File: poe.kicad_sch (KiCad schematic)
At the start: 50 parts

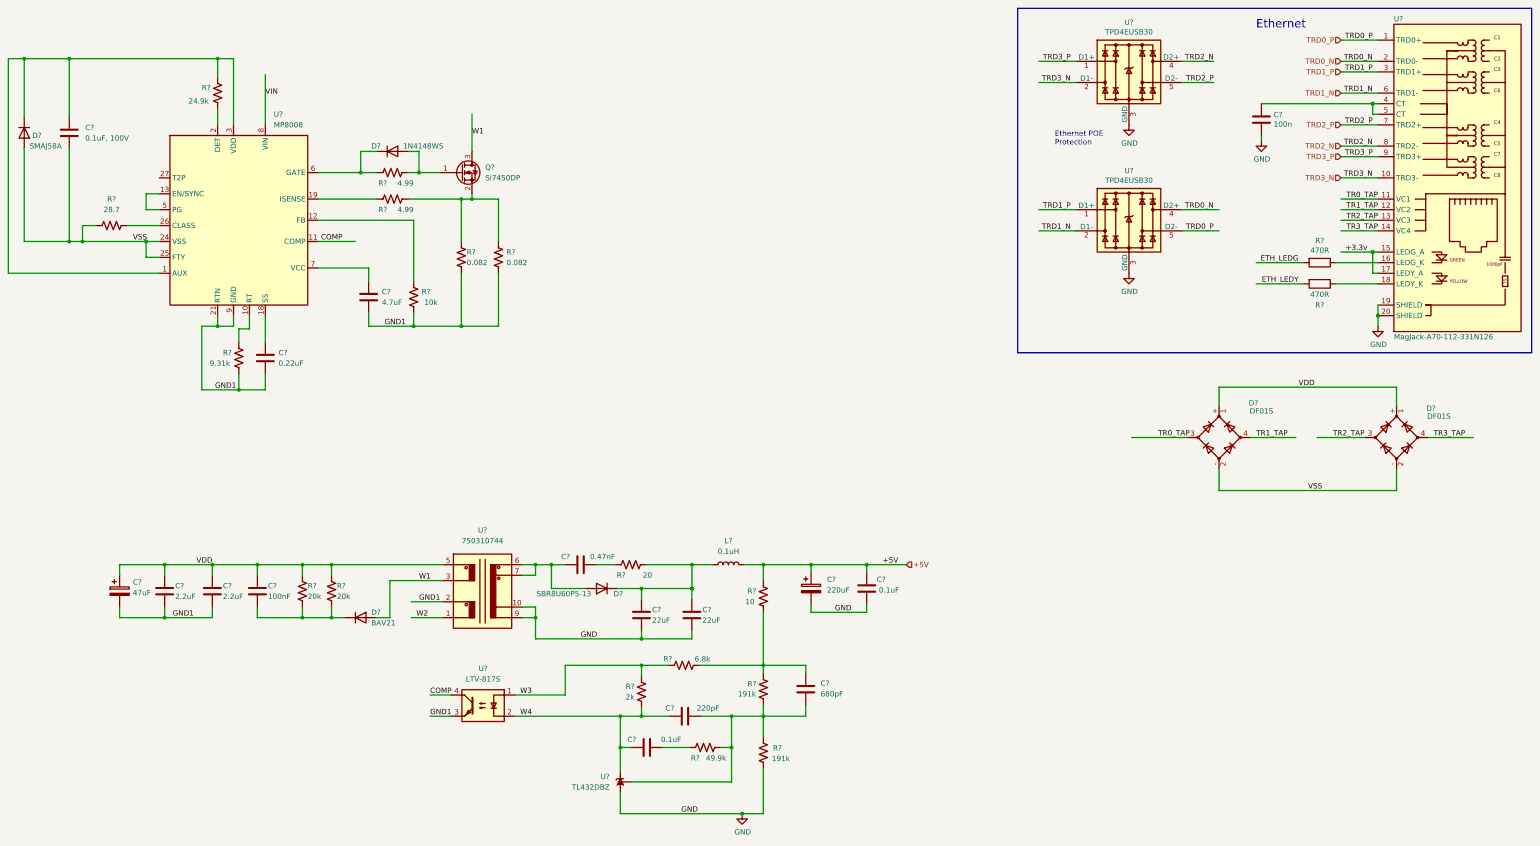
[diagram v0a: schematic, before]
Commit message: added M.2 m-key connector to schematic
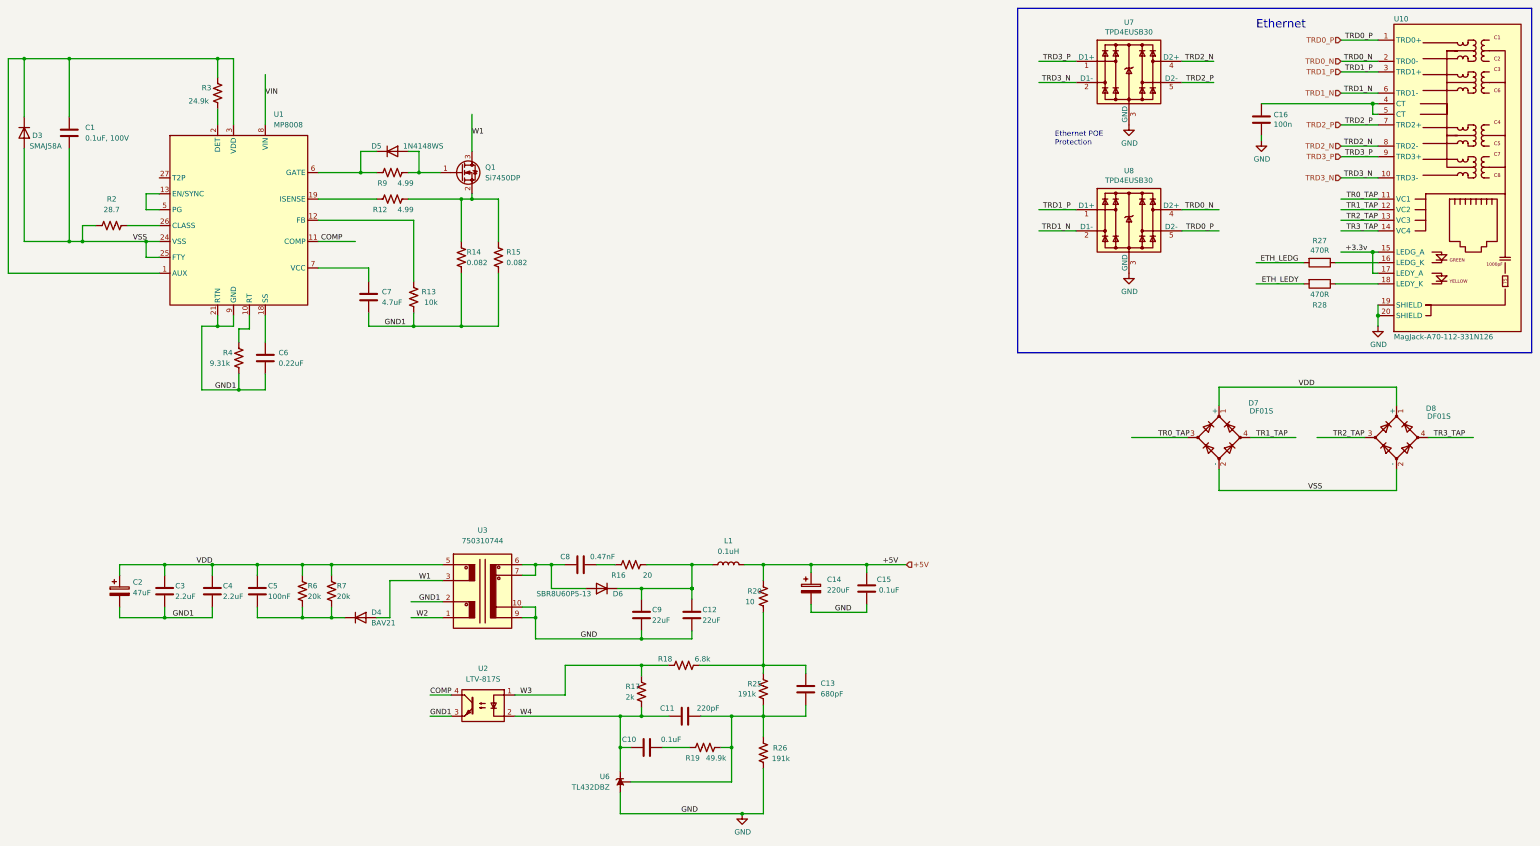
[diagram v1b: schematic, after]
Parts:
- gave numbers to parts that had none: 50

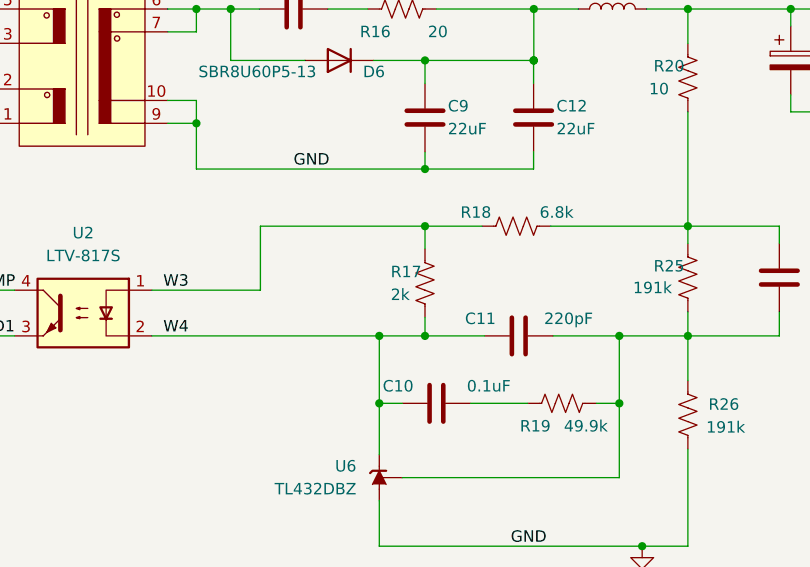
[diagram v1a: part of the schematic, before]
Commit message: removed unused components
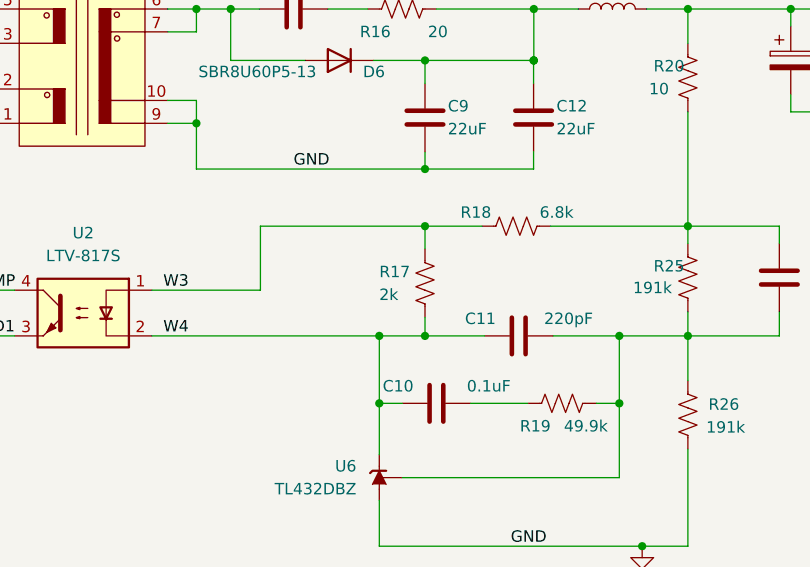
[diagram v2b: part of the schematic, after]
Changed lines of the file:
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@@
   (symbol (lib_id "Device:R_US") (at 185.42 180.34 180) (unit 1)
     (in_bom yes) (on_board yes)
-    (property "Reference" "R17" (id 0) (at 181.61 179.07 0)
+    (property "Reference" "R17" (id 0) (at 180.34 179.07 0)
       (effects (font (size 1.27 1.27)) (justify right))
     )
-    (property "Value" "2k" (id 1) (at 181.61 181.61 0)
+    (property "Value" "2k" (id 1) (at 180.34 181.61 0)
       (effects (font (size 1.27 1.27)) (justify right))
     )

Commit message: added the M.2 connector and MP8008 footprints
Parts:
- U1: footprint (none) -> bitcart:QFN-28_EP_4x5_Pitch0.5mm; ME (none) -> 946-MP8008GV-P
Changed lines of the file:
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@@
       (effects (font (size 1.27 1.27)) (justify left))
     )
-    (property "Footprint" "" (id 2) (at 87.63 66.04 0)
+    (property "Footprint" "bitcart:QFN-28_EP_4x5_Pitch0.5mm" (id 2) (at 87.63 66.04 0)
       (effects (font (size 1.27 1.27)) hide)
     )
-    (property "Datasheet" "" (id 3) (at 87.63 66.04 0)
+    (property "Datasheet" "https://www.mouser.com/datasheet/2/277/MP8008GV_Z-2946099.pdf" (id 3) (at 87.63 66.04 0)
       (effects (font (size 1.27 1.27)) hide)
     )
@@
       (effects (font (size 1.27 1.27)) hide)
     )
+    (property "ME" "946-MP8008GV-P" (id 5) (at 87.63 66.04 0)
+      (effects (font (size 1.27 1.27)) hide)
+    )

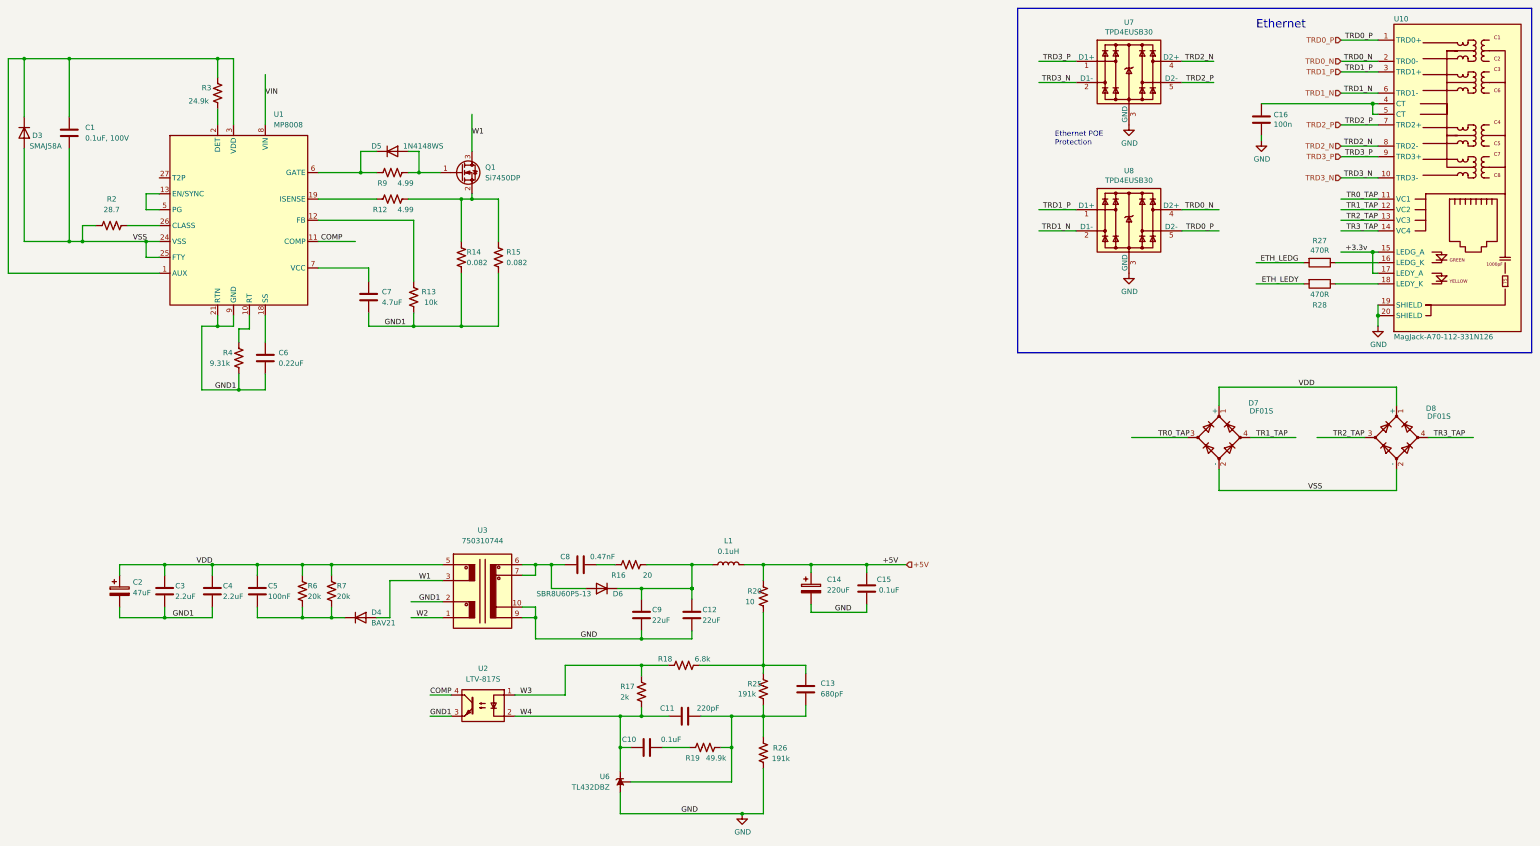
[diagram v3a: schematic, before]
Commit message: adding PoE parts
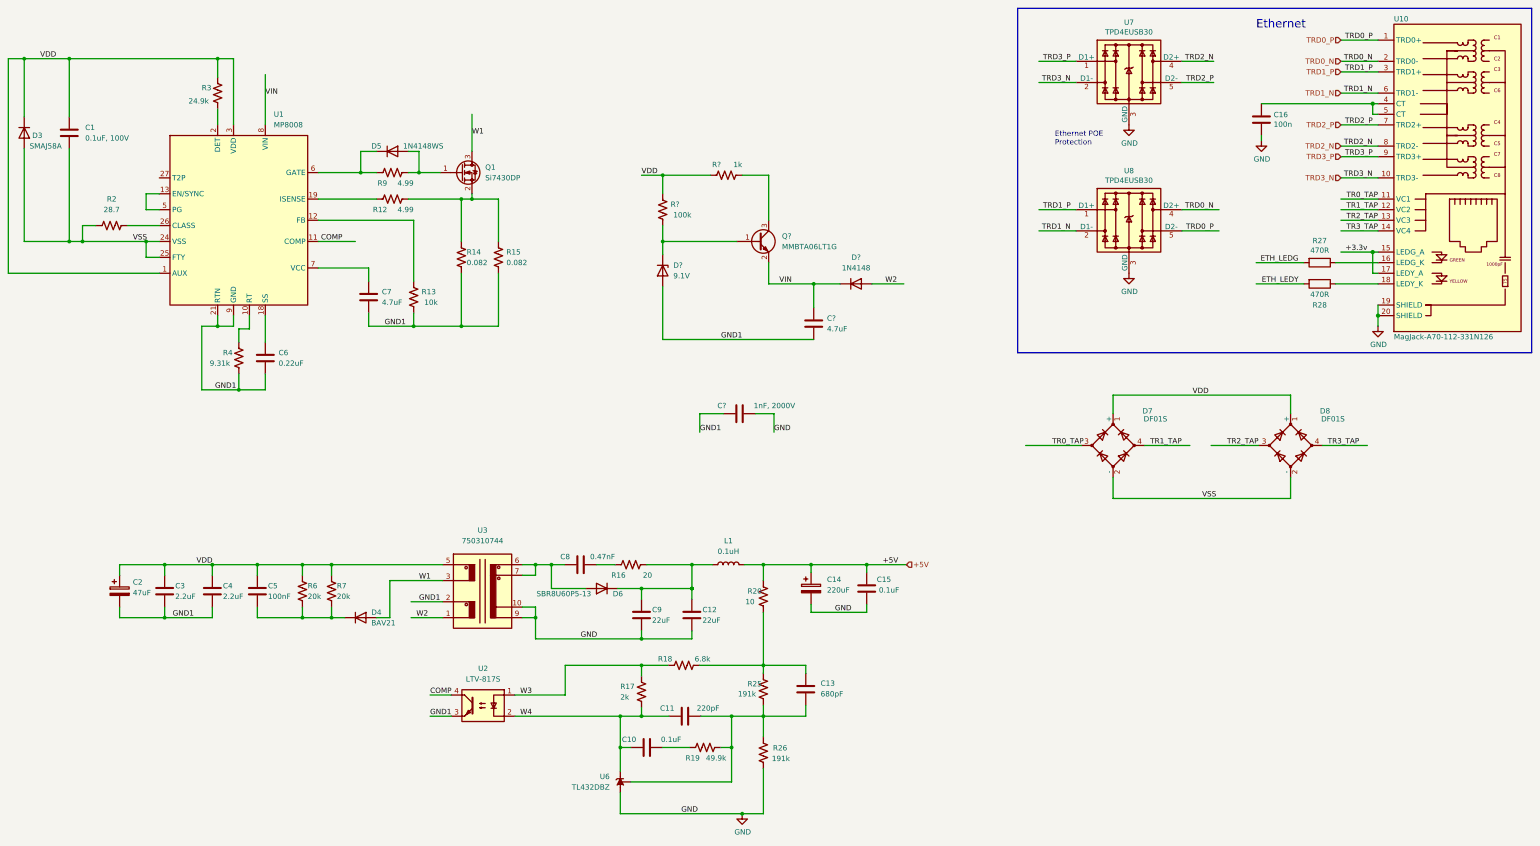
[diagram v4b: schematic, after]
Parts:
- added C?: 1nF, 2000V, symbol Device:C
- added C?: 4.7uF, symbol Device:C
- added D?: 9.1V, symbol Device:D_Zener
- added D?: 1N4148, Diode_THT:D_DO-35_SOD27_P7.62mm_Horizontal, symbol Diode:1N4148
- added Q?: MMBTA06LT1G, Package_TO_SOT_SMD:SOT-23, symbol Transistor_BJT:MMBTA42
- added R?: 1k, symbol Device:R_US
- added R?: 100k, symbol Device:R_US
- D7, D8: footprint (none) -> bitcart:DF01S; DK (none) -> DF01SCT-ND
- L1: footprint (none) -> bitcart:IND_744373240010; DK (none) -> 732-3344-1-ND; PARTNO (none) -> 744373240010
- Q1: value Si7450DP -> Si7430DP; footprint Package_TO_SOT_SMD:SOT-23 -> (none); ME (none) -> 781-SI7430DP-T1-GE3; PARTNO (none) -> SI7430DP-T1-GE3
- U3: footprint (none) -> bitcart:750310744
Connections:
- net GND: now also C?.2
- net GND1: now also C?.1, C?.2, D?.2 (A)
- net VDD: now also C1.1, D3.1 (K), R3.2, U1.1 (AUX), U1.3 (VDD), R?.2, R?.2
- net VIN: now also C?.1, D?.1 (K), Q?.2 (E)
- net W2: now also D?.2 (A)
- new net: Q?.3 (C), R?.1
- new net: D?.1 (K), Q?.1 (B), R?.1
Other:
- moved on the sheet: D7
